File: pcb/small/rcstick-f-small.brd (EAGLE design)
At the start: 15.4 x 40 mm, 41 parts, among them J1 MOLEX_48037-0001, J2 2212S, SW1 SKRPACE010, U1 STM32F042KT, U2 CC2500, U3 MCP1703AT-3302E/CB, X1 8MHz/15pF, X2 26MHz/9pF, X3 (50 Ohm)

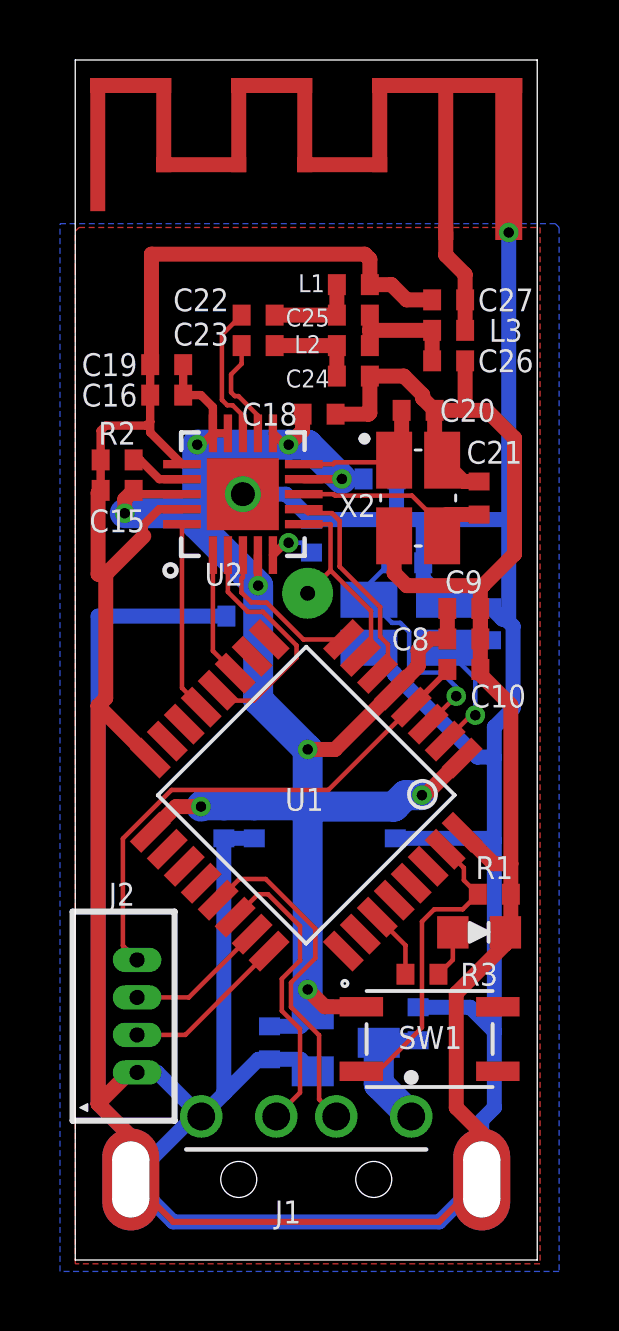
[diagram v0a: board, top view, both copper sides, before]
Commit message: renumbering capacities
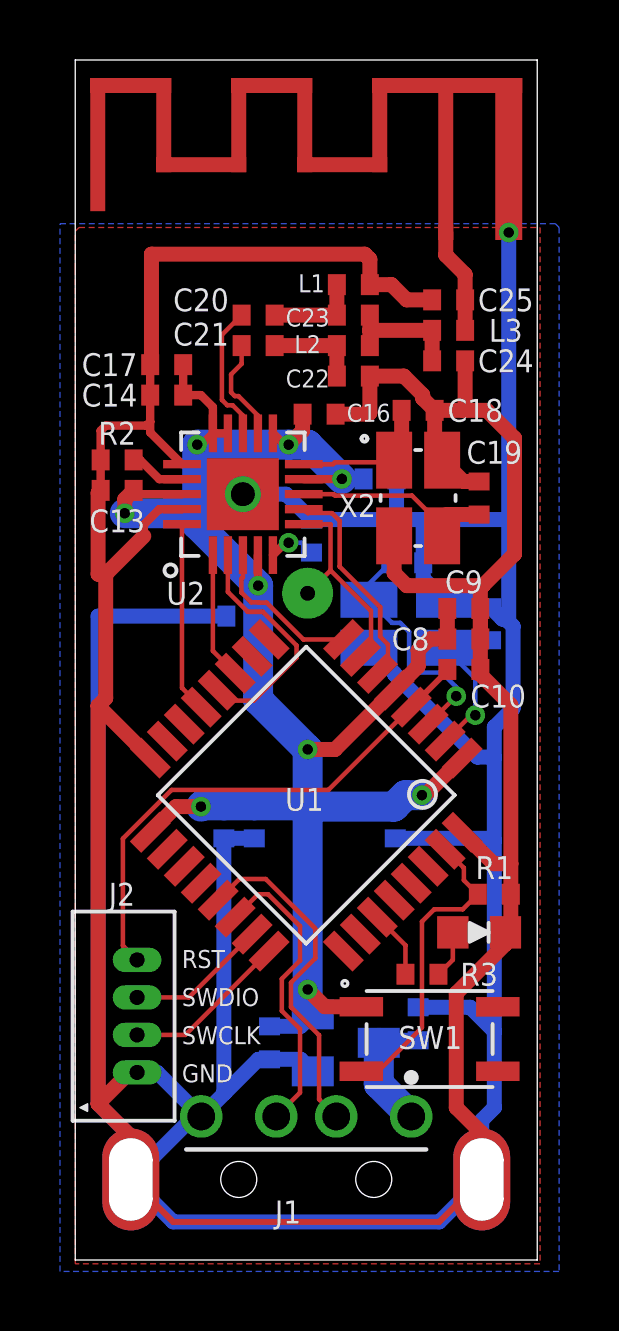
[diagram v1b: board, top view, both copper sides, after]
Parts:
- removed C26: 1.8p, gen-discrete3:RCL_C0402_HS
- removed C27: 1.5p, gen-discrete3:RCL_C0402_HS
- added C13, C14: 220p, gen-discrete3:RCL_C0402_HS
- C15, C16: value 220p -> 0.1u
- C17: value 0.1u -> 220p
- C18: value 0.1u -> 12p
- C19: value 220p -> 12p
- C20, C21: value 12p -> 100p
- C22, C23: value 100p -> 1p
- C24: value 1p -> 1.8p
- C25: value 1p -> 1.5p
- moved C19 11.3 mm to (13.5, 25.4), turned to 90 degrees
- moved C21 8.95 mm to (6.10, 30.5), turned to 0 degrees
- moved C15 8.77 mm to (10.2, 26.0), flipped to the bottom
- moved C17 8.07 mm to (3.05, 29.8), flipped to the top
- moved C20 6.21 mm to (6.10, 31.5)
- moved C16 5.12 mm to (8.13, 28.2), turned to 0 degrees
- moved C22 3.77 mm to (9.27, 29.5)
- moved C23 3.33 mm to (9.27, 31.5)
- moved C18 3.30 mm to (11.4, 28.3)
- moved C24 3.22 mm to (12.4, 30.0)
- moved C25 3.22 mm to (12.4, 32.0), turned to 180 degrees
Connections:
- net +3V3: now also C13.1, C14.1; no longer C18.1, C19.1
- net GND: now also C13.2, C14.2, C22.2, C25.2; no longer C20.2, C21.2, C26.2, C27.2
- net N$10: now also C23.2, C24.1; no longer C25.2, C26.1
- net N$11: now also C25.1; no longer C27.1
- net N$5: now also C20.2, C23.1; no longer C22.2, C25.1
- net N$9: now also C21.2, C22.1; no longer C23.2, C24.1
- net RF_N: now also C20.1; no longer C22.1
- net RF_P: now also C21.1; no longer C23.1
- net XOSC1: now also C19.1; no longer C21.1
- net XOSC2: now also C18.1; no longer C20.1
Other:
- outline, holes or cut-outs redrawn
- board text added: "GND"
- board text added: "RST"
- board text added: "SWCLK"
- board text added: "SWDIO"

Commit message: refine wiring
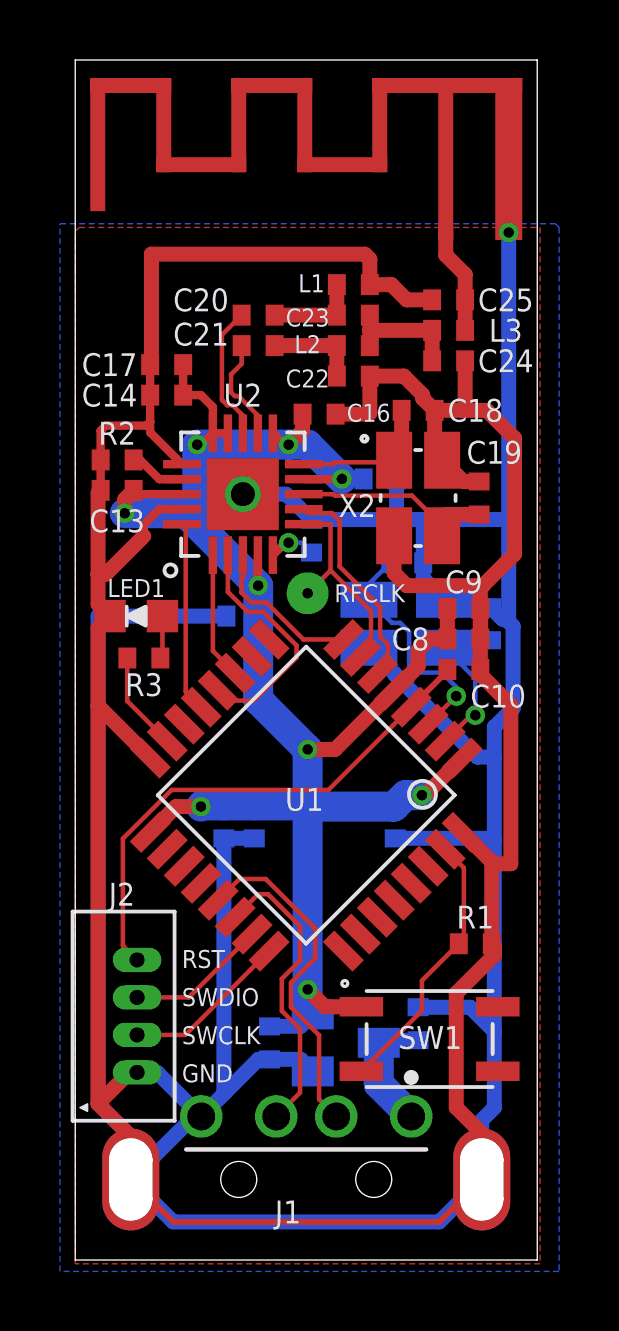
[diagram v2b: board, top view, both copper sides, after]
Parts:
- J1: device Molex - 48037-0001:MOLEX_48037-0001_1 -> Molex-48037-0001:MOLEX_48037-0001_1
- moved LED1 15.5 mm to (2.03, 21.5), turned to 180 degrees
- moved R3 14.0 mm to (2.29, 20.1)
- moved R1 1.77 mm to (13.3, 10.5)
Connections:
- net LED: now also U1.15; no longer U1.27
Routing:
- net BOOT0: track 10.3 -> 9.07 mm
- net LED: track 2.29 -> 3.32 mm
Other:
- board text added: "LED1"
- board text added: "RFCLK"

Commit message: minor update
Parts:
- X1: value 8MHz/15pF -> 16MHz/10pF
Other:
- board text added: "V1.0"
- board text added: "rcstick"
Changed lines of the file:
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@@
 <drawing>
 <settings>
-<setting alwaysvectorfont="yes"/>
+<setting alwaysvectorfont="no"/>
 <setting verticaltext="up"/>
 </settings>
@@
 </layers>
 <board>
-<fusionsync huburn="a.cGVyc29uYWw6dWUyYmE2M2My" projecturn="a.cGVyc29uYWw6dWUyYmE2M2MyIzIwMTgwOTE3MTQ5MTY5Mjgx" f3durn="urn:adsk.wipprod:dm.lineage:Ka2zEVxqQJuLWRWjQCtt5A" pcbguid="2642404a-56bf-401e-824e-11ebb673c24c" lastpulledtime="2019-02-23T02:20:42Z" lastsyncedchangeguid="14ffaf8c-116c-151d-89a5-ee57188373da"/>
+<fusionsync huburn="a.cGVyc29uYWw6dWUyYmE2M2My" projecturn="a.cGVyc29uYWw6dWUyYmE2M2MyIzIwMTgwOTE3MTQ5MTY5Mjgx" f3durn="urn:adsk.wipprod:dm.lineage:Ka2zEVxqQJuLWRWjQCtt5A" pcbguid="2642404a-56bf-401e-824e-11ebb673c24c" lastpulledtime="2019-02-23T02:20:42Z" lastsyncedchangeguid="c32bfccb-ff7c-c85a-67ed-160dc844cbdb"/>
 <plain>
 <dimension x1="0" y1="40" x2="0" y2="0" x3="-5.08" y3="20" textsize="1.778" layer="51"/>
@@
 <wire x1="0" y1="0" x2="15.4" y2="0" width="0" layer="20"/>
 <wire x1="15.4" y1="0" x2="15.4" y2="40" width="0" layer="20"/>
-<wire x1="12.95" y1="3.335" x2="14.15" y2="3.335" width="0.254" layer="20" curve="-180"/>
-<wire x1="14.15" y1="3.335" x2="14.15" y2="2.035" width="0.254" layer="20"/>
-<wire x1="14.15" y1="2.035" x2="12.95" y2="2.035" width="0.254" layer="20" curve="-180"/>
-<wire x1="12.95" y1="2.035" x2="12.95" y2="3.335" width="0.254" layer="20"/>
-<wire x1="1.25" y1="3.335" x2="2.45" y2="3.335" width="0.254" layer="20" curve="-180"/>
-<wire x1="2.45" y1="3.335" x2="2.45" y2="2.035" width="0.254" layer="20"/>
-<wire x1="2.45" y1="2.035" x2="1.25" y2="2.035" width="0.254" layer="20" curve="-180"/>
-<wire x1="1.25" y1="2.035" x2="1.25" y2="3.335" width="0.254" layer="20"/>
+<wire x1="12.95" y1="3.335" x2="14.15" y2="3.335" width="0" layer="20" curve="-180"/>
+<wire x1="14.15" y1="3.335" x2="14.15" y2="2.035" width="0" layer="20"/>
+<wire x1="14.15" y1="2.035" x2="12.95" y2="2.035" width="0" layer="20" curve="-180"/>
+<wire x1="12.95" y1="2.035" x2="12.95" y2="3.335" width="0" layer="20"/>
+<wire x1="1.25" y1="3.335" x2="2.45" y2="3.335" width="0" layer="20" curve="-180"/>
+<wire x1="2.45" y1="3.335" x2="2.45" y2="2.035" width="0" layer="20"/>
+<wire x1="2.45" y1="2.035" x2="1.25" y2="2.035" width="0" layer="20" curve="-180"/>
+<wire x1="1.25" y1="2.035" x2="1.25" y2="3.335" width="0" layer="20"/>
 <text x="3.556" y="6.223" size="0.6" layer="25" font="vector" align="center-left">GND</text>
 <text x="3.556" y="10.033" size="0.6" layer="25" font="vector" align="center-left">RST</text>
@@
 <text x="8.636" y="22.225" size="0.6" layer="25" font="vector" align="center-left">RFCLK</text>
 <text x="2.032" y="22.098" size="0.6" layer="25" font="vector" align="bottom-center">LED1</text>
+<text x="14.732" y="30.607" size="2.5" layer="22" rot="MR0">rcstick</text>
+<text x="4.064" y="30.607" size="1.2" layer="22" font="vector" rot="MR0">V1.0</text>
 </plain>
 <attributes>
@@
 </element>
 <element name="J1" library="Molex-48037-0001" library_urn="urn:adsk.eagle:library:9157828" package="MOLEX_48037-0001_1" package3d_urn="urn:adsk.eagle:package:9157833/2" value="MOLEX_48037-0001" x="7.7" y="-5.715" smashed="yes">
-<attribute name="NAME" x="7.092" y="1.221" size="0.762" layer="25" font="vector" align="bottom-center"/>
+<attribute name="NAME" x="7.727" y="1.475" size="0.762" layer="25" font="vector" align="bottom-center"/>
 </element>
 <element name="J2" library="connector" library_urn="urn:adsk.eagle:library:5418080" package="53047-0410" package3d_urn="urn:adsk.eagle:package:5418110/2" value="2212S" x="2.062" y="8.128" smashed="yes" rot="R270">
@@
 <attribute name="VALUE" x="5.842" y="5.334" size="1.016" layer="28" rot="MR90"/>
 </element>
-<element name="X1" library="CRYSTAL3225" library_urn="urn:adsk.eagle:library:8815235" package="CRYSTAL3225-HS" package3d_urn="urn:adsk.eagle:package:8815239/2" value="8MHz/15pF" x="11.049" y="21.209" smashed="yes" rot="MR0">
+<element name="X1" library="CRYSTAL3225" library_urn="urn:adsk.eagle:library:8815235" package="CRYSTAL3225-HS" package3d_urn="urn:adsk.eagle:package:8815239/2" value="16MHz/10pF" x="11.049" y="21.209" smashed="yes" rot="MR0">
 <attribute name="NAME" x="11.049009375" y="18.79600625" size="0.762" layer="26" font="vector" rot="MR0" align="bottom-center"/>
 <attribute name="VALUE" x="11.049009375" y="18.54200625" size="1.016" layer="28" font="vector" rot="MR0" align="center"/>
